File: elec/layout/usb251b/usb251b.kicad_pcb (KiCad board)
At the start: 2 copper layers, 17 parts

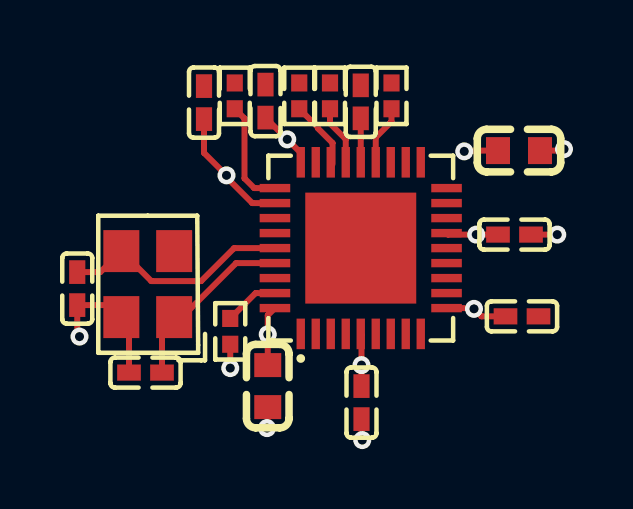
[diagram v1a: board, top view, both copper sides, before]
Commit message: Cleanup layout for usb hub and usb-uart, add CM5 controller heatsink outline
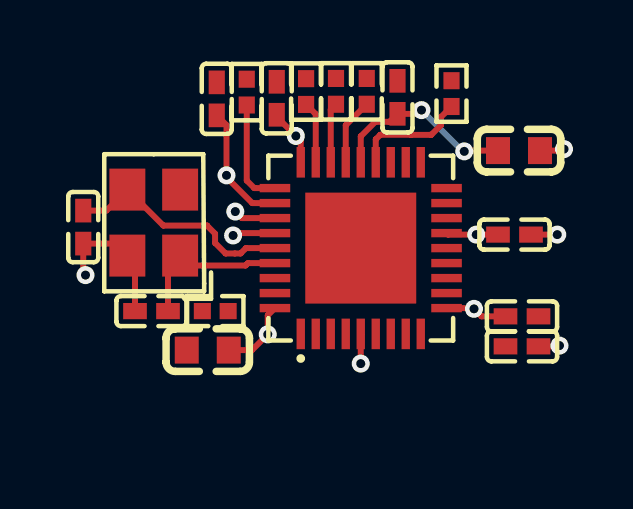
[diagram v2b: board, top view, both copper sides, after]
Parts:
- added R6: 10kΩ ±1% 62.5mW, atopile:R0402-56259e, F.Cu at (165.5, 101.3)
- C1, C2: value 10µF ±10% 10V X5R -> 10µF ±20% 6.3V X5R
- moved C4 5.67 mm to (172.7, 109.8), turned to 0 degrees
- moved C2 2.33 mm to (162.2, 109.9), turned to 180 degrees
- moved X1 2.06 mm to (160.4, 105.7)
- moved C10 2.06 mm to (158.1, 105.8)
- moved C9 2.06 mm to (160.3, 108.6)
- moved R2 2.00 mm to (170.3, 101.4)
- moved C8 1.23 mm to (168.6, 101.5)
- moved R1 1.23 mm to (167.5, 101.3)
- moved R4 1.23 mm to (166.5, 101.3)
- moved R3 0.84 mm to (162.5, 108.6), turned to 180 degrees
- moved C5 0.44 mm to (162.5, 101.5)
- moved R5 0.42 mm to (163.5, 101.3)
- moved C3 0.39 mm to (164.5, 101.5)
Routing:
- net hv: track 16.4 -> 19.8 mm, vias 7 -> 8
- net RESET_N: track 0.00 -> 2.06 mm
- net SDA_SMBBATA_NON_REM1: track 2.00 -> 3.91 mm
- net RBIAS: track 1.84 -> 0.00 mm
- net gnd: track 8.58 -> 7.08 mm, vias 6 -> 4
- net USBDP_UP: track 0.00 -> 1.43 mm, vias 0 -> 1
- net USBDM_UP: track 0.00 -> 1.41 mm, vias 0 -> 1
- net xin: track 6.12 -> 5.61 mm
